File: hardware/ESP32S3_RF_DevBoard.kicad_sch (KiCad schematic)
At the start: 33 parts, among them J1 USB4105-GF-A, J2 Conn_01x22, J3 Conn_01x22, SW1 BOOT, SW2 RESET, U1 ESD122DMYR, U2 LD1117DT33CTR, U3 ESP32-S3-WROOM-1-N8

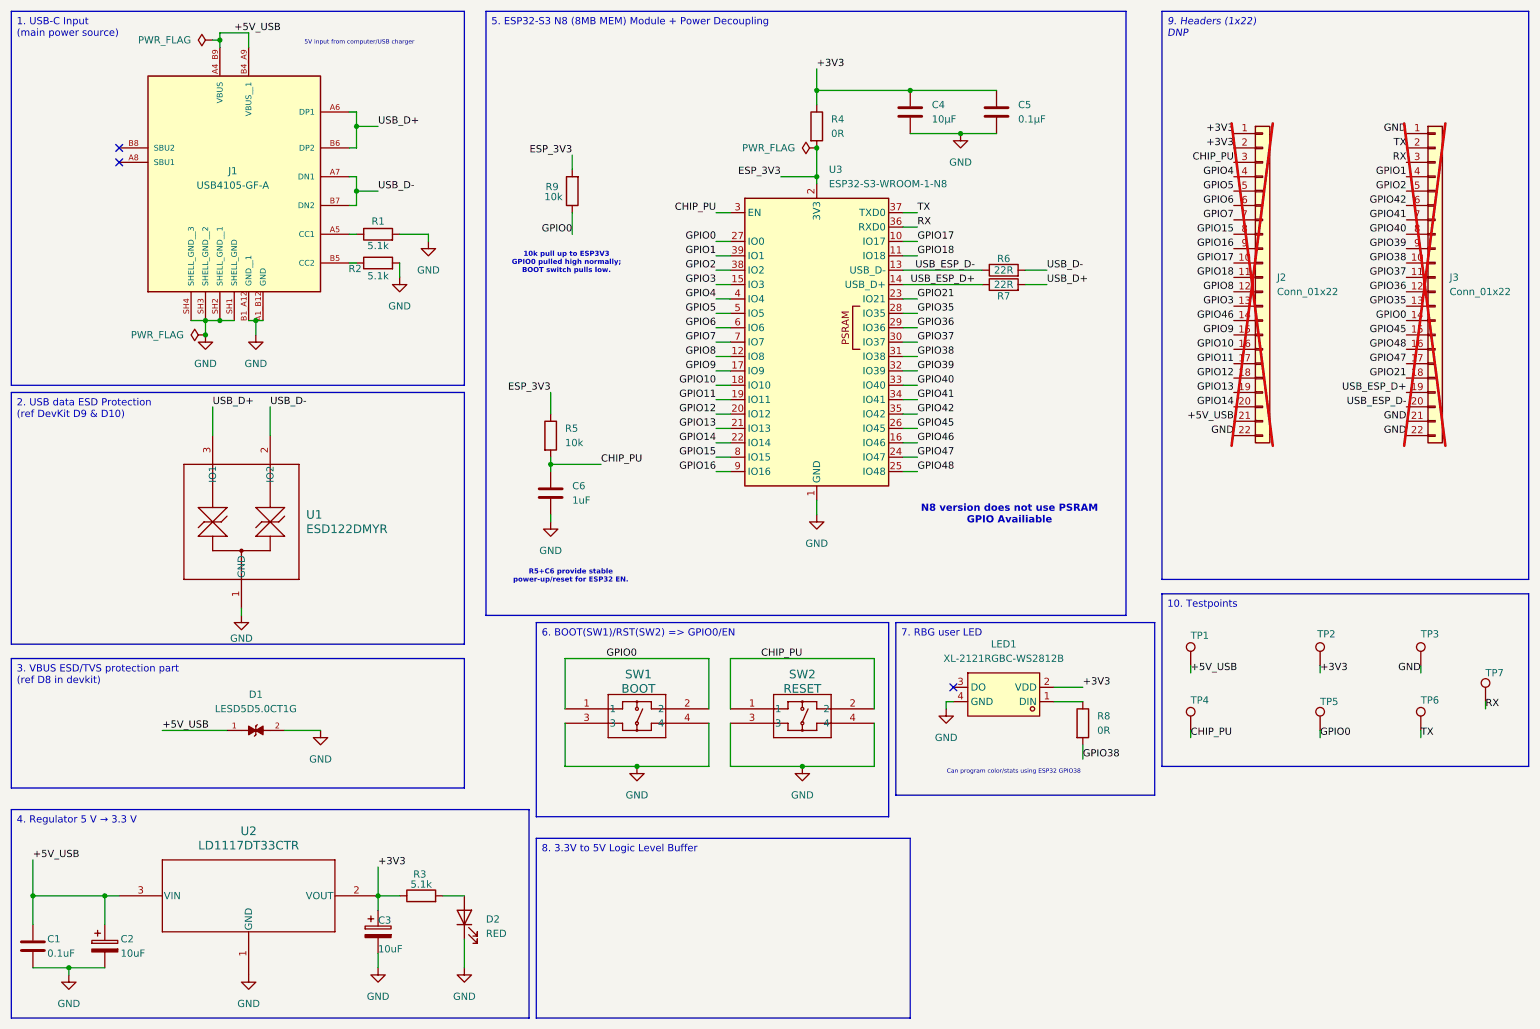
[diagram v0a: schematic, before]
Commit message: finalizing the schematic and double checking connections and proper decoupling CAP
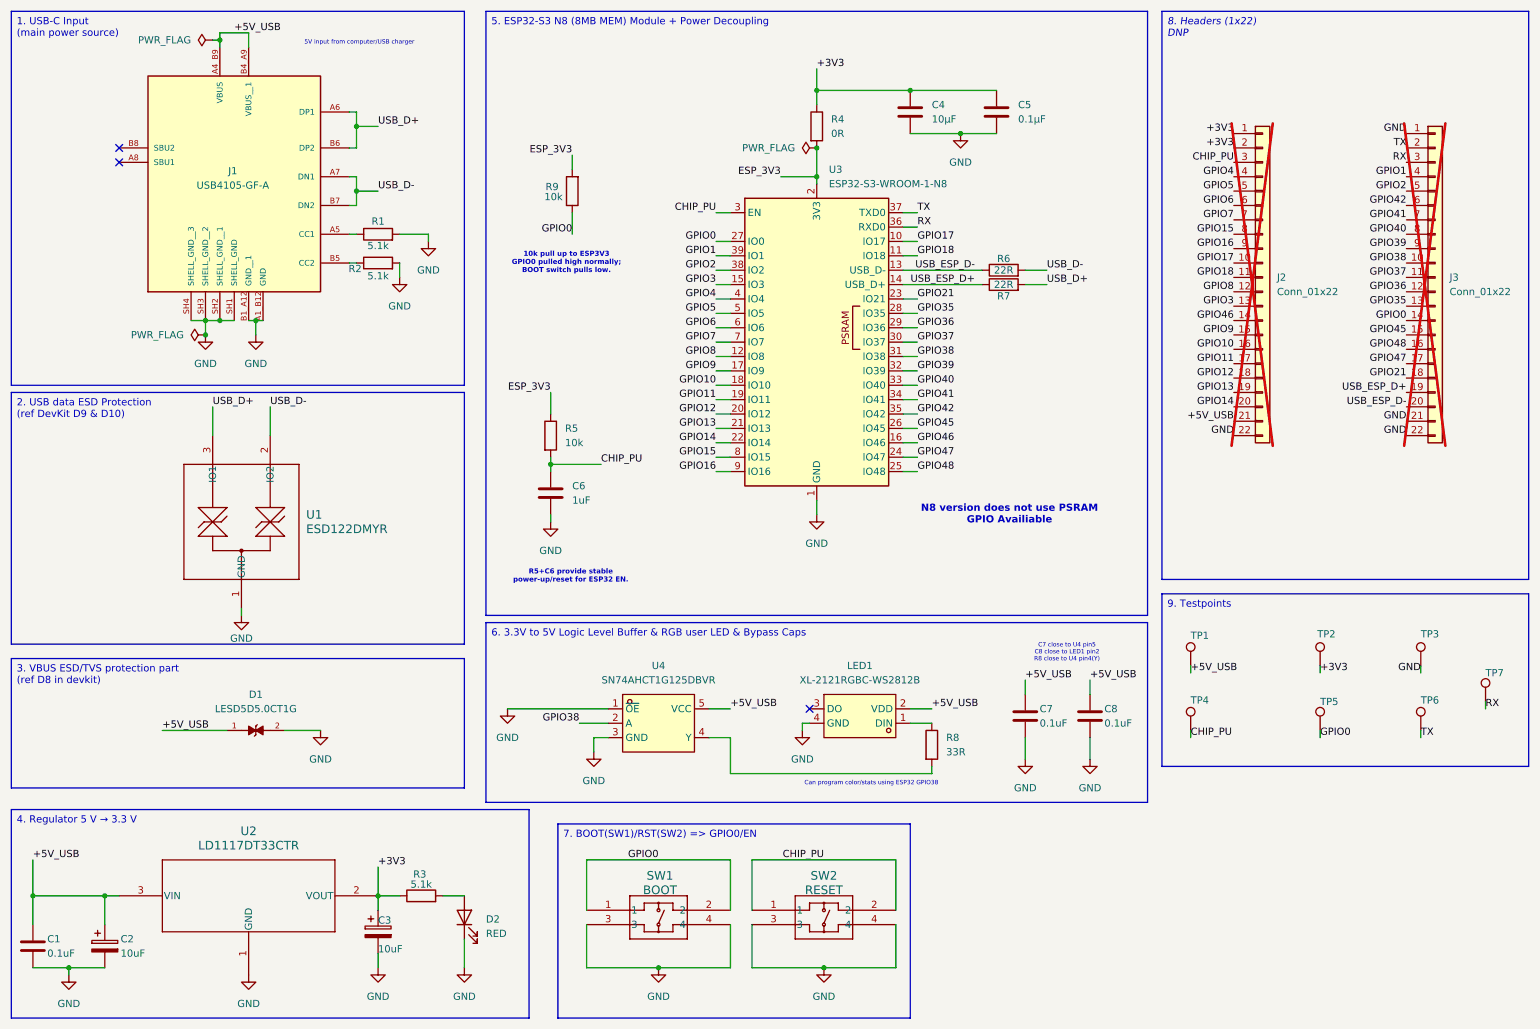
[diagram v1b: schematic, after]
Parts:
- added C7, C8: 0.1uF, Capacitor_SMD:C_0603_1608Metric, symbol Device:C
- added U4: SN74AHCT1G125DBVR, easyeda:SOT-23-5_L3.0-W1.7-P0.95-LS2.8-BR, symbol easyeda:SN74AHCT1G125DBVR
- R8: value 0R -> 33R; LCSC/JLCPCB C21189 -> C23140; MPN (none) -> 0603WAF330JT5E
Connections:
- net +3V3: no longer LED1.2 (VDD)
- net +5V_USB: now also LED1.2 (VDD), C7.1, C8.1, U4.5 (VCC)
- net GND: now also C7.2, C8.2, U4.1 (~{OE}), U4.3 (GND)
- net GPIO38: now also U4.2 (A); no longer R8.2
- new net: R8.2, U4.4 (Y)
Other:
- note added: "C7 close to U4 pin5 C8 close to LED1 pin2 R8 close to U4 pin4(Y)"
- moved on the sheet: LED1, R8, SW1, SW2

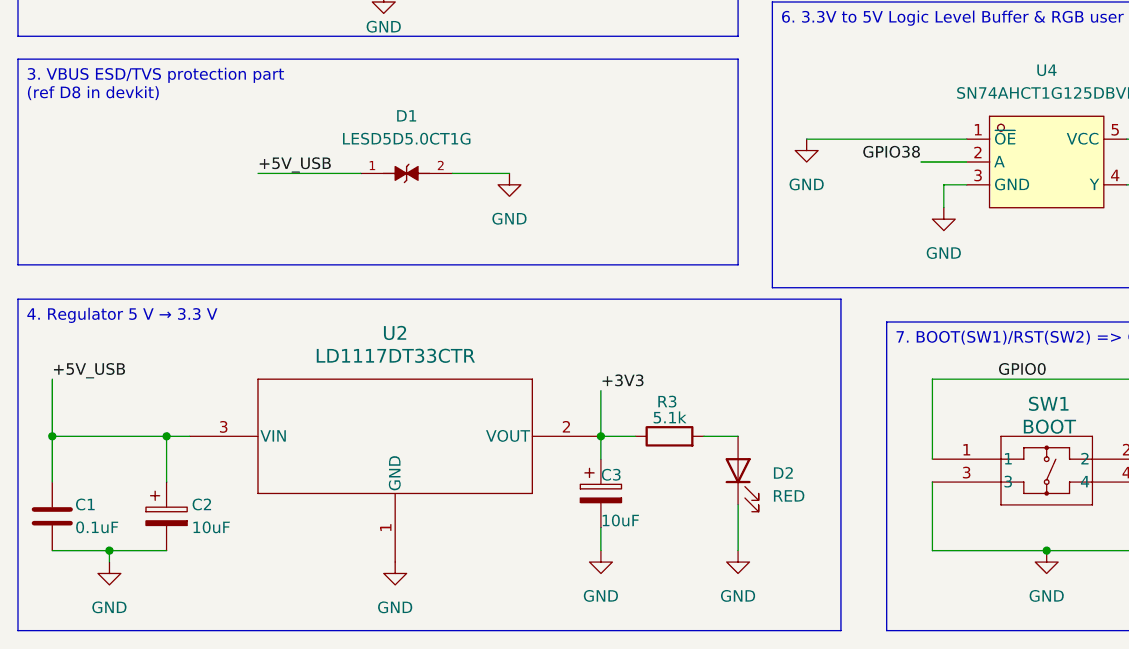
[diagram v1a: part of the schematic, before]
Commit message: going through schematic for connections and running ERC - as of now ERC is clean
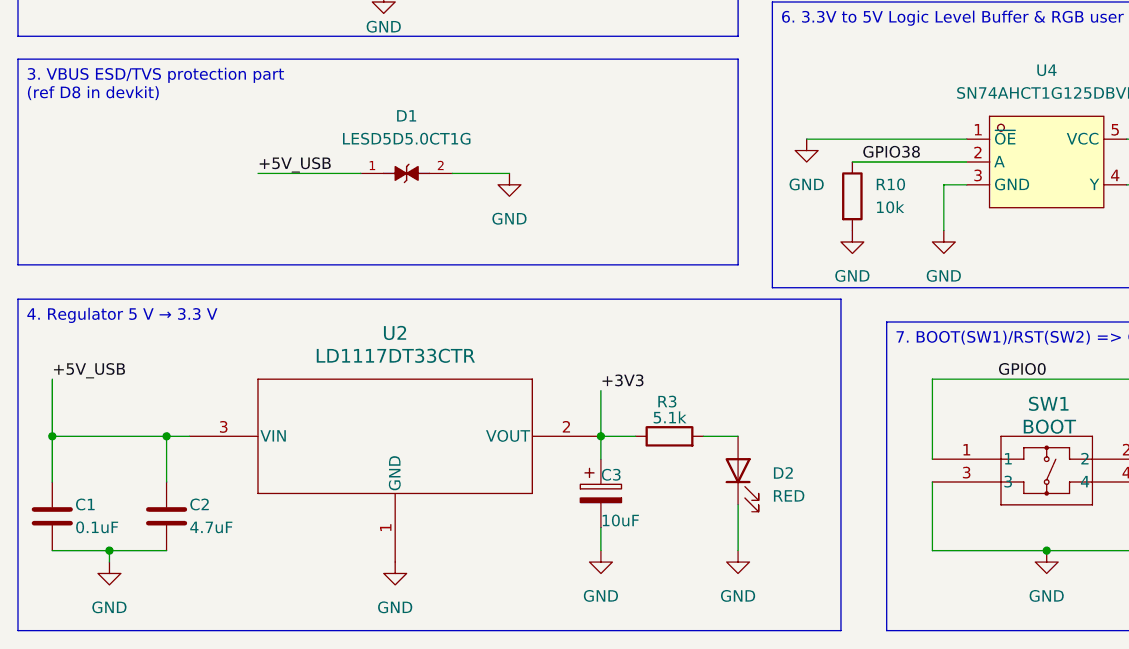
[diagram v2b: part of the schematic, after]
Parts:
- removed C2: 10uF, Capacitor_Tantalum_SMD:CP_EIA-3528-21_Kemet-B, symbol Device:C_Polarized
- added C2: 4.7uF, Capacitor_SMD:C_0805_2012Metric, symbol Device:C
- added R10: 10k, Resistor_SMD:R_0603_1608Metric, symbol Device:R
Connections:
- net +5V_USB: now also C2.1
- net GND: now also C2.2, R10.2
- net GPIO38: now also R10.1

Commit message: placement of all components and editing skilscreen rules
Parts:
- TP1, TP2, TP3: footprint TestPoint:TestPoint_Pad_D1.0mm -> TestPoint:TestPoint_Pad_D1.5mm
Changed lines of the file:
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@@
 			)
 		)
-		(property "Footprint" "TestPoint:TestPoint_Pad_D1.0mm"
+		(property "Footprint" "TestPoint:TestPoint_Pad_D1.5mm"
 			(at 267.97 130.81 0)
 			(hide yes)
@@
 			)
 		)
-		(property "Footprint" "TestPoint:TestPoint_Pad_D1.0mm"
+		(property "Footprint" "TestPoint:TestPoint_Pad_D1.5mm"
 			(at 227.33 130.81 0)
 			(hide yes)
@@
 			)
 		)
-		(property "Footprint" "TestPoint:TestPoint_Pad_D1.0mm"
+		(property "Footprint" "TestPoint:TestPoint_Pad_D1.5mm"
 			(at 250.19 130.81 0)
 			(hide yes)
@@
 			)
 		)
-		(property "Description" ""
+		(property "Description" "https://jlcpcb.com/partdetail/STMicroelectronics-LD1117DT33CTR/C36395"
 			(at 33.02 170.18 0)
 			(hide yes)

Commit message: - 5 unconnected components as of now! - trying to route the rest of the GPIO and CHIP_PU traces - will deal with silkscreen and footprint warnings last !
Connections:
- net CHIP_PU: now also J2.4 (Pin_4); no longer J2.3 (Pin_3)
- net GPIO1: now also J3.2 (Pin_2); no longer J3.4 (Pin_4)
- net GPIO2: now also J3.3 (Pin_3); no longer J3.5 (Pin_5)
- net GPIO37: now also J3.10 (Pin_10); no longer J3.11 (Pin_11)
- net GPIO38: now also J3.11 (Pin_11); no longer J3.10 (Pin_10)
- net GPIO4: now also J2.3 (Pin_3); no longer J2.4 (Pin_4)
- net RX: now also J3.5 (Pin_5); no longer J3.3 (Pin_3)
- net TX: now also J3.4 (Pin_4); no longer J3.2 (Pin_2)
- net USB_ESP_D+: no longer J3.19 (Pin_19)
- net USB_ESP_D-: no longer J3.20 (Pin_20)
- no-connect marks 3 -> 5
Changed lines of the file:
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@@
+	)
+	(no_connect
+		(at 260.35 82.55)
 	)
 	(no_connect
@@
 	)
 	(no_connect
+		(at 260.35 85.09)
+	)
+	(no_connect
 		(at 33.02 39.37)
 	)
@@
 	)
 	(label "GPIO1"
-		(at 260.35 44.45 180)
+		(at 260.35 39.37 180)
 		(effects
 			(font
@@
 	)
 	(label "GPIO4"
-		(at 229.87 44.45 180)
+		(at 229.87 41.91 180)
 		(effects
 			(font
@@
 	)
 	(label "TX"
-		(at 260.35 39.37 180)
+		(at 260.35 44.45 180)
 		(effects
 			(font
@@
 	)
 	(label "GPIO38"
-		(at 260.35 59.69 180)
+		(at 260.35 62.23 180)
 		(effects
 			(font
@@
 		)
 	)
-	(label "USB_ESP_D+"
-		(at 260.35 82.55 180)
-		(effects
-			(font
-				(size 1.27 1.27)
-			)
-			(justify right bottom)
-		)
-	)
 	(label "GPIO35"
 		(at 173.99 68.58 0)
@@
 	)
 	(label "RX"
-		(at 260.35 41.91 180)
+		(at 260.35 46.99 180)
 		(effects
 			(font
@@
 	)
 	(label "CHIP_PU"
-		(at 229.87 41.91 180)
+		(at 229.87 44.45 180)
 		(effects
 			(font
@@
 	)
 	(label "GPIO2"
-		(at 260.35 46.99 180)
+		(at 260.35 41.91 180)
 		(effects
 			(font
@@
 		)
 	)
-	(label "USB_ESP_D-"
-		(at 260.35 85.09 180)
-		(effects
-			(font
-				(size 1.27 1.27)
-			)
-			(justify right bottom)
-		)
-	)
 	(label "GPIO41"
 		(at 173.99 83.82 0)
@@
 	)
 	(label "GPIO37"
-		(at 260.35 62.23 180)
-		(effects
-			(font
+		(at 260.35 59.69 180)
+		(effects
+			(font

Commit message: working on silkscreen warnings and fixing . - all routing complete (0 unconnections) - verfiy in JLCPCB USB NPTH hole placeement (may have to exclude the error if JLCPCB clears through dfm)
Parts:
- removed TP6, TP7: TestPoint, TestPoint:TestPoint_Pad_D1.0mm, symbol Connector:TestPoint
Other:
- moved on the sheet: TP3
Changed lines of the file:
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@@
 	(wire
 		(pts
-			(xy 262.89 132.08) (xy 262.89 130.81)
+			(xy 265.43 137.16) (xy 265.43 135.89)
 		)
 		(stroke
@@
 	(wire
 		(pts
-			(xy 274.32 138.43) (xy 274.32 137.16)
-		)
-		(stroke
-			(width 0)
-			(type default)
-		)
-	)
-	(wire
-		(pts
 			(xy 193.04 60.96) (xy 196.85 60.96)
 		)
@@
 	(wire
 		(pts
-			(xy 262.89 143.51) (xy 262.89 142.24)
-		)
-		(stroke
-			(width 0)
-			(type default)
-		)
-	)
-	(wire
-		(pts
 			(xy 171.45 60.96) (xy 185.42 60.96)
 		)
@@
 		)
 	)
-	(label "TX"
-		(at 262.89 143.51 0)
-		(effects
-			(font
-				(size 1.27 1.27)
-			)
-			(justify left bottom)
-		)
-	)
 	(label "GPIO4"
 		(at 229.87 41.91 180)
@@
 		)
 	)
-	(label "RX"
-		(at 274.32 138.43 0)
-		(effects
-			(font
-				(size 1.27 1.27)
-			)
-			(justify left bottom)
-		)
-	)
 	(label "+3V3"
 		(at 78.74 166.37 0)
@@
 	)
 	(label "GND"
-		(at 262.89 132.08 180)
+		(at 265.43 137.16 180)
 		(effects
 			(font
@@
 	(symbol
 		(lib_id "Connector:TestPoint")
-		(at 262.89 130.81 0)
+		(at 265.43 135.89 0)
 		(unit 1)
 		(body_style 1)
@@
 		(dnp no)
 		(property "Reference" "TP3"
-			(at 262.89 125.222 0)
+			(at 265.43 130.302 0)
 			(show_name no)
 			(do_not_autoplace no)
@@
 		)
 		(property "Value" "TestPoint"
-			(at 265.43 128.7779 0)
+			(at 267.97 133.8579 0)
 			(hide yes)
 			(show_name no)
@@
 		)
 		(property "Footprint" "TestPoint:TestPoint_Pad_D1.5mm"
-			(at 267.97 130.81 0)
+			(at 270.51 135.89 0)
 			(hide yes)
 			(show_name no)
@@
 		)
 		(property "Datasheet" ""
-			(at 267.97 130.81 0)
+			(at 270.51 135.89 0)
 			(hide yes)
 			(show_name no)
@@
 		)
 		(property "Description" "test point"
-			(at 262.89 130.81 0)
+			(at 265.43 135.89 0)
 			(hide yes)
 			(show_name no)
@@
 	)
 	(symbol
-		(lib_id "Connector:TestPoint")
-		(at 274.32 137.16 0)
-		(unit 1)
-		(body_style 1)
-		(exclude_from_sim no)
-		(in_bom no)
-		(on_board yes)
-		(in_pos_files no)
-		(dnp no)
-		(property "Reference" "TP7"
-			(at 274.32 132.08 0)
-			(show_name no)
-			(do_not_autoplace no)
-			(effects
-				(font
-					(size 1.27 1.27)
-				)
-				(justify left)
-			)
-		)
-		(property "Value" "TestPoint"
-			(at 276.86 135.1279 0)
-			(hide yes)
-			(show_name no)
-			(do_not_autoplace no)
-			(effects
-				(font
-					(size 1.27 1.27)
-				)
-				(justify left)
-			)
-		)
-		(property "Footprint" "TestPoint:TestPoint_Pad_D1.0mm"
-			(at 279.4 137.16 0)
-			(hide yes)
-			(show_name no)
-			(do_not_autoplace no)
-			(effects
-				(font
-					(size 1.27 1.27)
-				)
-			)
-		)
-		(property "Datasheet" ""
-			(at 279.4 137.16 0)
-			(hide yes)
-			(show_name no)
-			(do_not_autoplace no)
-			(effects
-				(font
-					(size 1.27 1.27)
-				)
-			)
-		)
-		(property "Description" "test point"
-			(at 274.32 137.16 0)
-			(hide yes)
-			(show_name no)
-			(do_not_autoplace no)
-			(effects
-				(font
-					(size 1.27 1.27)
-				)
-			)
-		)
-		(pin "1"
-		)
-		(instances
-			(project "ESP32S3_RF_DevBoard"
-				(path "/784333dd-3fa1-4922-bbbf-658c1720cebd"
-					(reference "TP7")
-					(unit 1)
-				)
-			)
-		)
-	)
-	(symbol
 		(lib_id "Device:R")
 		(at 86.36 171.45 90)
@@
 					(unit 1)
 				)
-			)
-		)
-	)
-	(symbol
-		(lib_id "Connector:TestPoint")
-		(at 262.89 142.24 0)
-		(unit 1)
-		(body_style 1)
-		(exclude_from_sim no)
-		(in_bom no)
-		(on_board yes)
-		(in_pos_files no)
-		(dnp no)
-		(property "Reference" "TP6"
-			(at 262.89 136.906 0)
-			(show_name no)
-			(do_not_autoplace no)
-			(effects
-				(font
-					(size 1.27 1.27)
-				)
-				(justify left)
-			)
-		)
-		(property "Value" "TestPoint"
-			(at 265.43 140.2079 0)
-			(hide yes)
-			(show_name no)
-			(do_not_autoplace no)
-			(effects
-				(font
-					(size 1.27 1.27)
-				)
-				(justify left)
-			)
-		)
-		(property "Footprint" "TestPoint:TestPoint_Pad_D1.0mm"
-			(at 267.97 142.24 0)
-			(hide yes)
-			(show_name no)
-			(do_not_autoplace no)
-			(effects
-				(font
-					(size 1.27 1.27)
-				)
-			)
-		)
-		(property "Datasheet" ""
-			(at 267.97 142.24 0)
-			(hide yes)
-			(show_name no)
-			(do_not_autoplace no)
-			(effects
-				(font
-					(size 1.27 1.27)
-				)
-			)
-		)
-		(property "Description" "test point"
-			(at 262.89 142.24 0)
-			(hide yes)
-			(show_name no)
-			(do_not_autoplace no)
-			(effects
-				(font
-					(size 1.27 1.27)
-				)
-			)
-		)
-		(pin "1"
-		)
-		(instances
-			(project "ESP32S3_RF_DevBoard"
-				(path "/784333dd-3fa1-4922-bbbf-658c1720cebd"
-					(reference "TP6")
-					(unit 1)
-				)

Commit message: - checking the drc - checking manufacturing for the USB receptacle - checking diff routing (diff imp check) rerouted - adding imgs a - adding in gerbers and drill files
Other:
- title: (none) -> ESP32 S3 RF Dev Board - Antoinette K.
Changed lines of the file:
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@@
 	(paper "A4")
 	(title_block
+		(title "ESP32 S3 RF Dev Board - Antoinette K.")
 		(date "2026-08-20")
 		(rev "v1")
